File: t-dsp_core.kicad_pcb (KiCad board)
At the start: 4 copper layers, 100 x 61 mm, 176 parts, among them IC1 Logic Level Shifter - 74HCT2G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, J1 J_PWR, J10 J_DMX, J11 J_LED, J12 J_ETH, J13 u.FL DNP (IDC767 ext-antenna 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, J2 J_TDM, J3 J_T, J4 J_USB, J5 J_MIDI, J7 J_SAI2, J8 J_S3, Q1 AO3401A, T108 Tab, T109 Tab, T110 Tab, T111 Tab, U1 Teensy 4.1 - DEVKIT, U11 Dual Buffer - SN74LVC2G125DCTR, U13 ESP32-S3-WROOM-1-N16R8, U15 LT3045EMSE#TRPBF, U16 THVD1450DR, U17 ISO7762DW, U18 TEA1-0505HI, U19 SN74LVC257APWR, U20 SN74LVC2G125DCTR, U21 SN74LVC244APWR, U22 IDC777-1, U23 SN74LVC138APWR, U24 AP63203WU, U4 Optoisolators - H11L1SM - 6-S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, U5 SN74LVC541APWR, U6 SN74LVC2G125DCTR, U7 SN74LVC2G125DCTR, U9 Dual Buffer - 74HCT2G17GW,125, Y1 24.576MHz

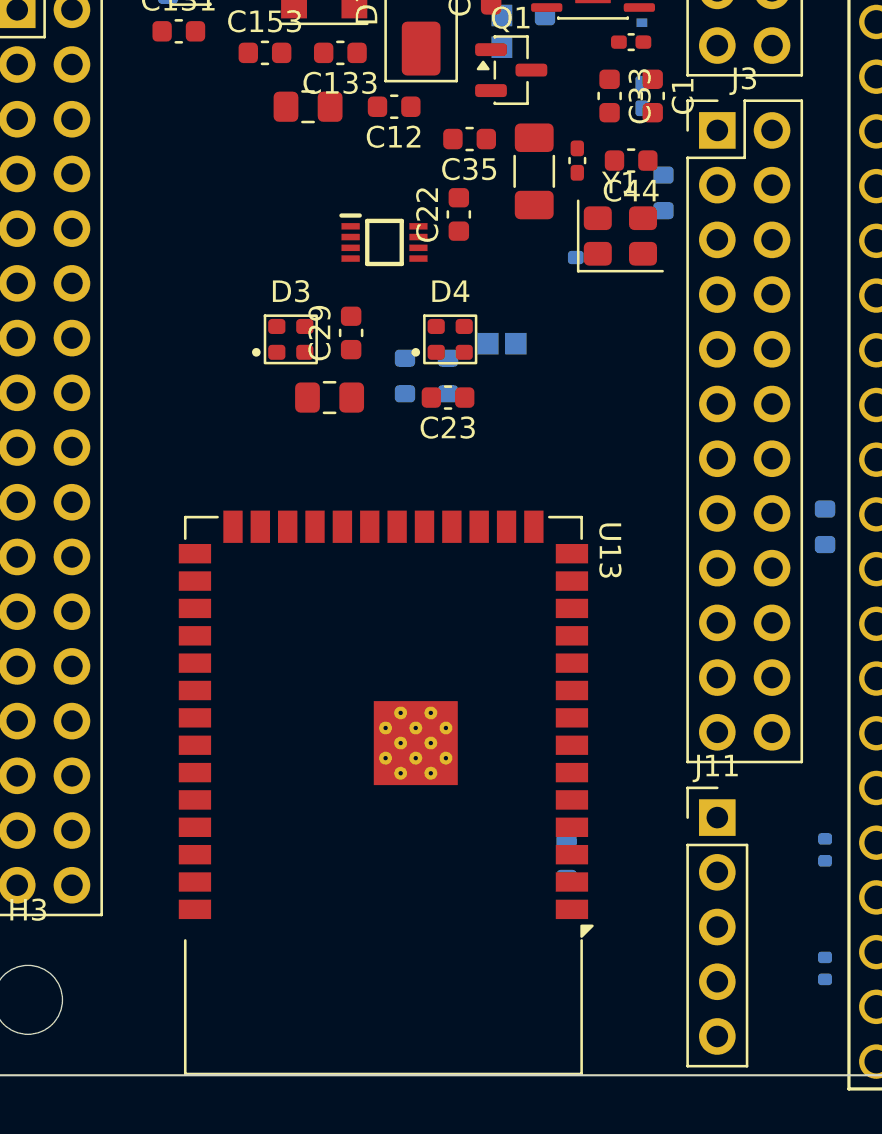
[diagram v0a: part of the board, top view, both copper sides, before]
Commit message: Board: user placement edits (J11 beside the LED driver, U13 nudged)
Co-Authored-By: Claude Fable 5.1 <noreply@anthropic.com>
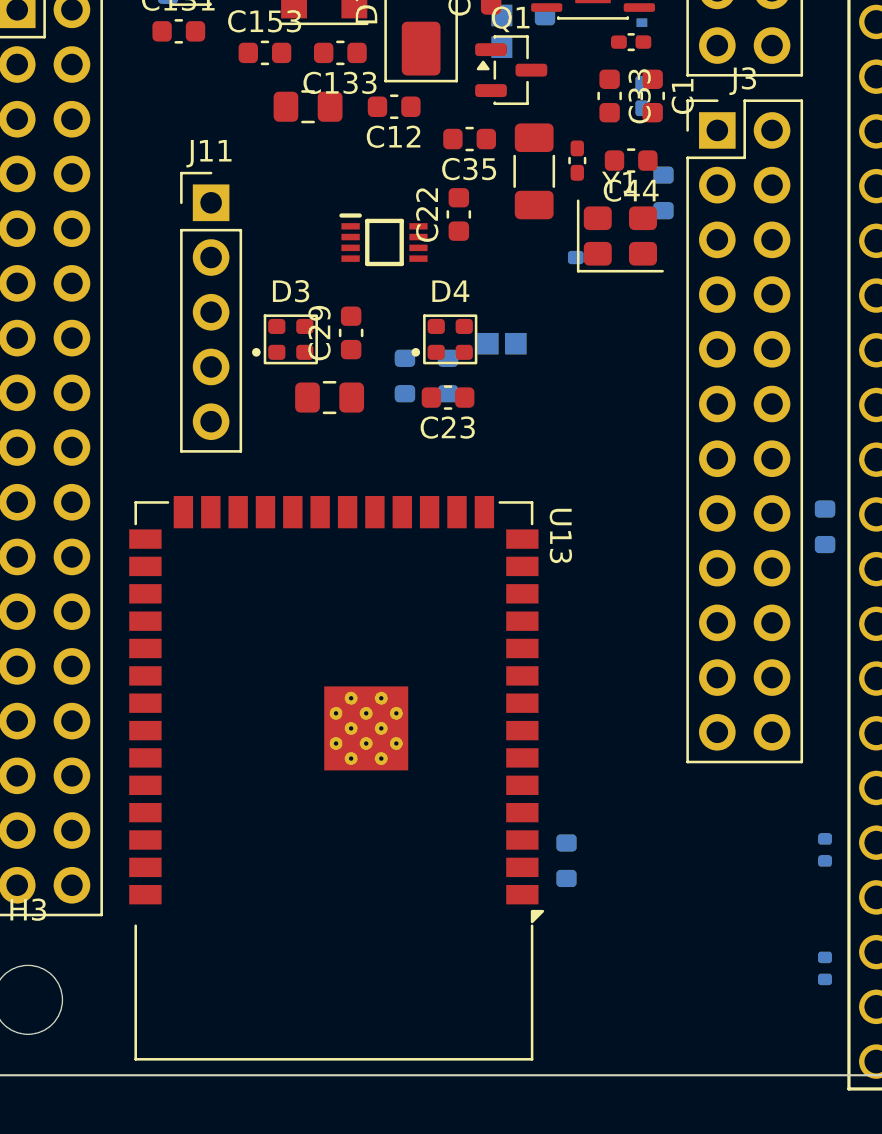
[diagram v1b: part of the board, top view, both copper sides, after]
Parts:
- moved J11 37.0 mm to (112.0, 159.5)
- moved U13 2.40 mm to (117.7, 186.4)
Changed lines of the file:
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@@
 	(footprint "RF_Module:ESP32-S3-WROOM-1"
 		(layer "F.Cu")
-		(at 120 187.04 180)
+		(at 117.7 186.36 180)
 		(descr "2.4 GHz Wi-Fi and Bluetooth module  https://www.espressif.com/sites/default/files/documentation/esp32-s3-wroom-1_wroom-1u_datasheet_en.pdf")
 		(tags "2.4 GHz Wi-Fi and Bluetooth module")
@@
 			(polygon
 				(pts
-					(xy 144 193.79) (xy 96 193.79) (xy 96 214.79) (xy 144 214.79)
+					(xy 141.7 193.11) (xy 93.7 193.11) (xy 93.7 214.11) (xy 141.7 214.11)
 				)
 			)
@@
 	(footprint "Connector_PinHeader_2.54mm:PinHeader_1x05_P2.54mm_Vertical"
 		(layer "F.Cu")
-		(at 135.5 188.04)
+		(at 112 159.5)
 		(descr "Through hole straight pin header, 1x05, 2.54mm pitch, single row")
 		(tags "Through hole pin header THT 1x05 2.54mm single row")

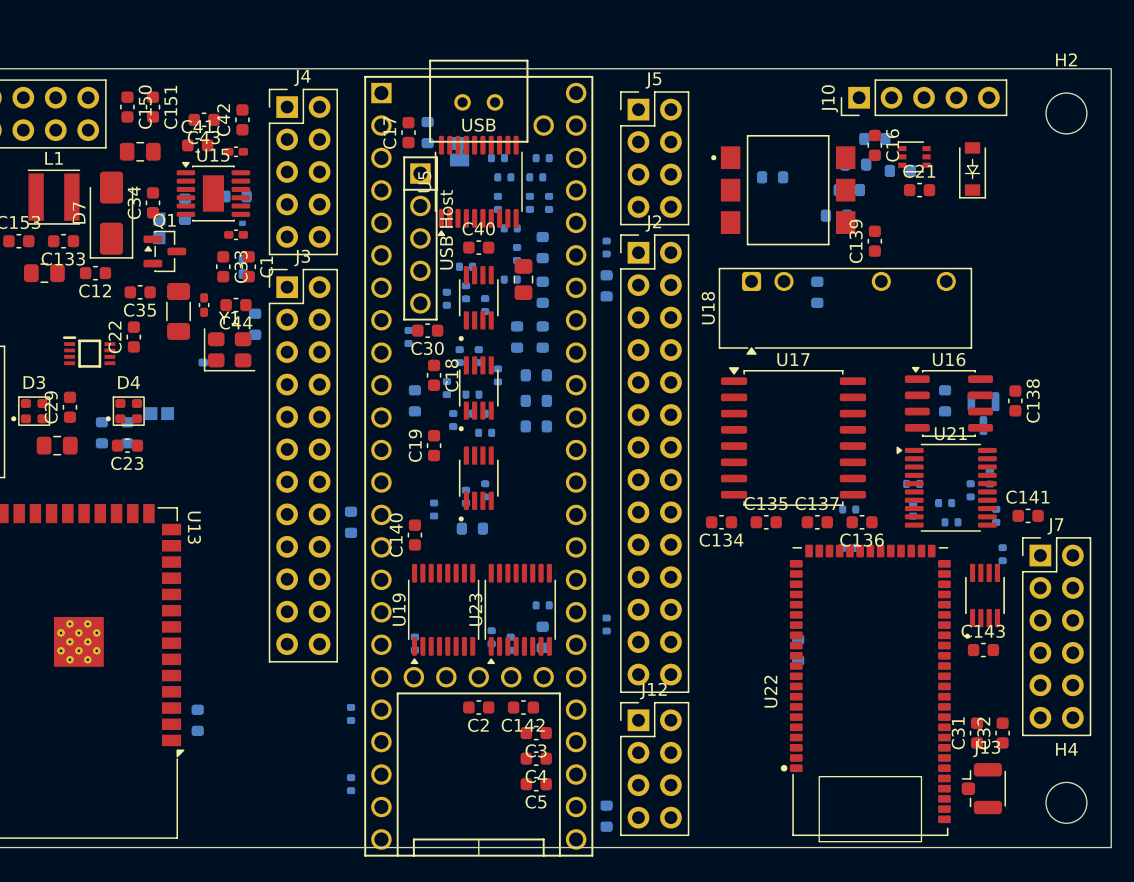
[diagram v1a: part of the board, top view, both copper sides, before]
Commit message: Spin 2 stage 10z (2/2, board): DMX footprints removed, J10 2x4 beside the S3, slot 3 re-planned, IDC777 antenna keep-out
- U16/U17/U18/D6/R71/C134-C139 removed; J10 is PinHeader_2x04 on row B at Y 49 (where J11 was before the user moved it to the LED block).
- Slot 3: MIDI at the top (U4, U9, D2), U21 header buffer at (83.0, 27.5) beside J_SAI2, IDC777 unchanged. No isolation barrier on the core any more.
- Rule area IDC777_ANT on all four copper layers (X 77.1-85.2, Y 55.4 to the edge): no tracks, vias or pours under the BT antenna.
- 123 passives re-placed (median 2.4 mm, mean 3.3 mm to their pin, 7 beyond 10 mm). DRC with parity: only the S3 module antenna courtyard (vs H3, J10), its 0.2 mm via holes and the outline footprint.

Co-Authored-By: Claude Fable 5.1 <noreply@anthropic.com>
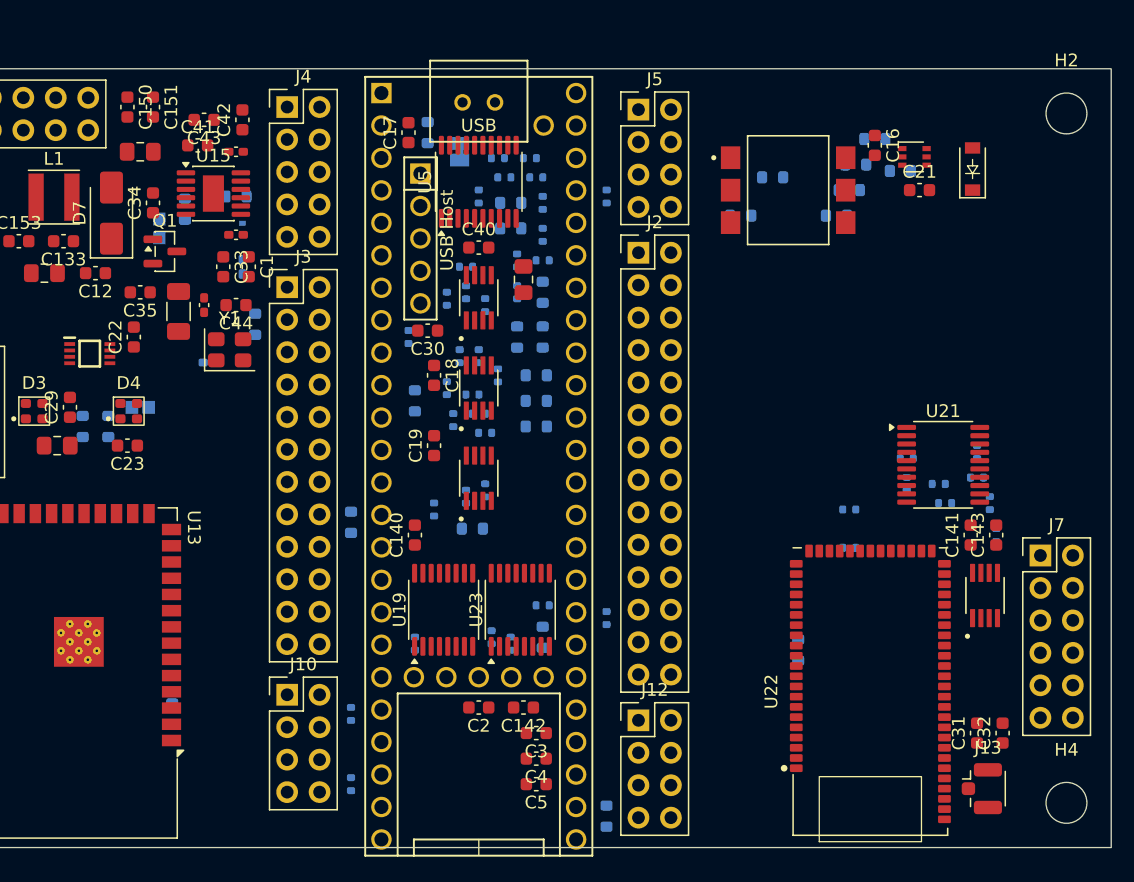
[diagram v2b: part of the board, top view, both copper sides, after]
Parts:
- removed C134, C136, C137: 100nF, Capacitor_SMD:C_0603_1608Metric
- removed C135, C138, C139: 10uF, Capacitor_SMD:C_0603_1608Metric
- removed D6: SM712, Package_TO_SOT_SMD:SOT-23
- removed R71: 120 DNP, Resistor_SMD:R_0603_1608Metric
- removed U16: THVD1450DR, Package_SO:SOIC-8_3.9x4.9mm_P1.27mm
- removed U17: ISO7762DW, Package_SO:SOIC-16W_7.5x10.3mm_P1.27mm
- removed U18: TEA1-0505HI, Converter_DCDC:Converter_DCDC_TRACO_TEA1-xxxxHI_THT
- J10: footprint Connector_PinHeader_2.54mm:PinHeader_1x05_P2.54mm_Vertical -> Connector_PinHeader_2.54mm:PinHeader_2x04_P2.54mm_Vertical
- moved J10 64.7 mm to (135.5, 188.0), turned to 0 degrees
- moved C143 9.06 mm to (191.0, 175.5), turned to 90 degrees
- moved R37 8.75 mm to (153.0, 151.5), turned to 180 degrees
- moved R35 8.49 mm to (171.0, 150.5), turned to 180 degrees
- moved R6 7.07 mm to (153.5, 154.0)
- moved R7 5.83 mm to (160.5, 149.0), turned to -90 degrees
- moved C141 4.74 mm to (189.0, 175.5), turned to 90 degrees
- moved R39 4.30 mm to (153.0, 149.5), turned to 180 degrees
- moved R45 3.81 mm to (154.5, 146.0), turned to 0 degrees
- moved R46 2.55 mm to (155.5, 152.0), turned to -90 degrees
- moved R92 2.24 mm to (189.5, 169.0)
- moved R47 2.06 mm to (155.5, 154.0), turned to 0 degrees
- moved R73 2.06 mm to (126.5, 189.5)
- moved R95 2.06 mm to (184.0, 171.5)
- moved R96 2.06 mm to (184.0, 169.5), turned to 0 degrees
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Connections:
- J10 pad 1: DMX_GND -> GND
- J10 pad 2: /DMX_A -> GND
- J10 pad 3: /DMX_B -> DMX_TX
- J10 pad 4: DMX_GND -> DMX_RX
- J10 pad 5: 5V_ISO -> DMX_DE

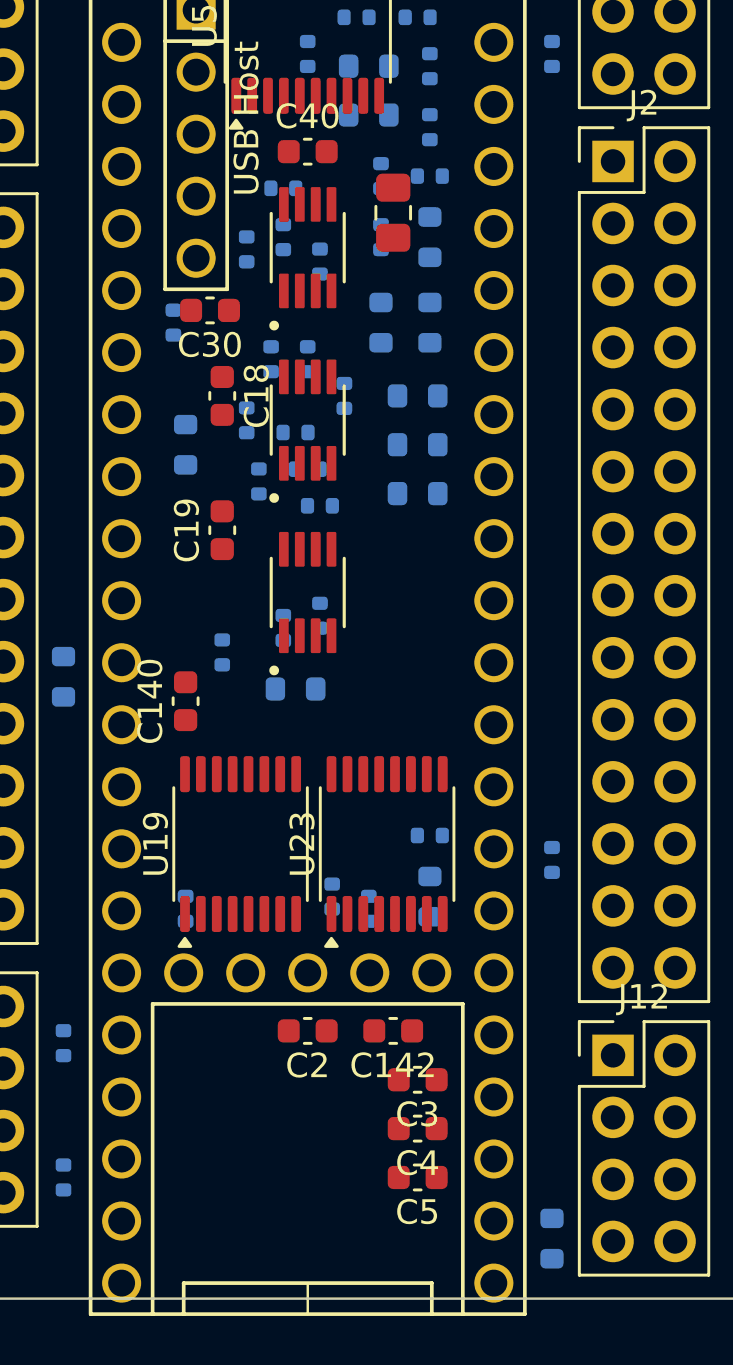
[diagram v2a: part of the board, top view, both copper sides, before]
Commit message: User edits: Teensy footprint to project_fp:Teensy41 (Ethernet pads), board saved from the PCB Editor
Co-Authored-By: Claude Fable 5.1 <noreply@anthropic.com>
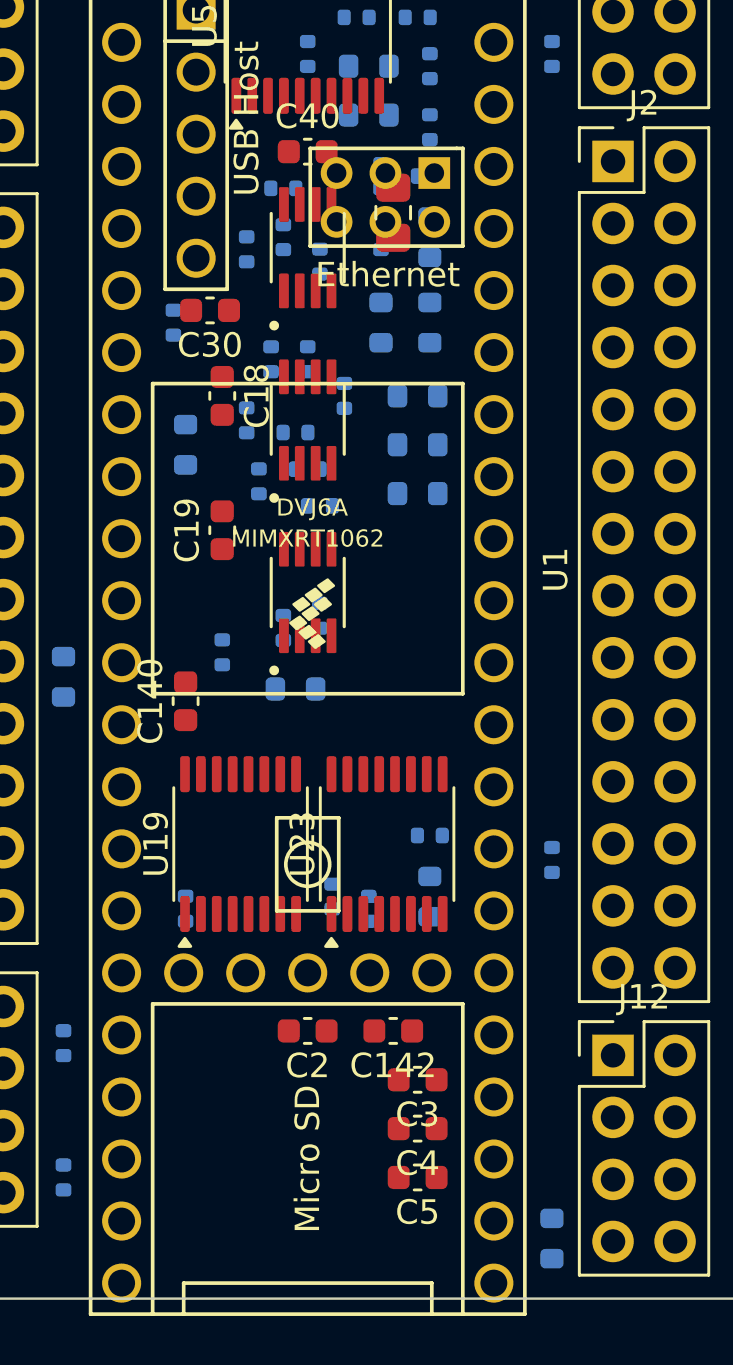
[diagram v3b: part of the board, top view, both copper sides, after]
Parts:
- U1: footprint project_fp:Teensy41_mod3 -> project_fp:Teensy41
